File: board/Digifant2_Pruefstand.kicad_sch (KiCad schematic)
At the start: 71 parts, among them J0 VW ECU HARNESS, J1 12V BENCH IN, J2 IDLE VALVE N71, J3 OLED / UI I2C, Q1 2N7002, Q2 P-MOS -30V >=5A, Q3 2N7002, Q5 2N7002, SW1 PUSH, SW2 PUSH, SW3 PUSH, U1 INA226 (0x40), U2 MCP4728 (0x60), U3 INA226 (0x41), U4 AD9833, U5 Raspberry Pi Pico, U6 TS5A3159A, U7 TS5A3159A, U8 TS5A3159A, Y1 25MHz

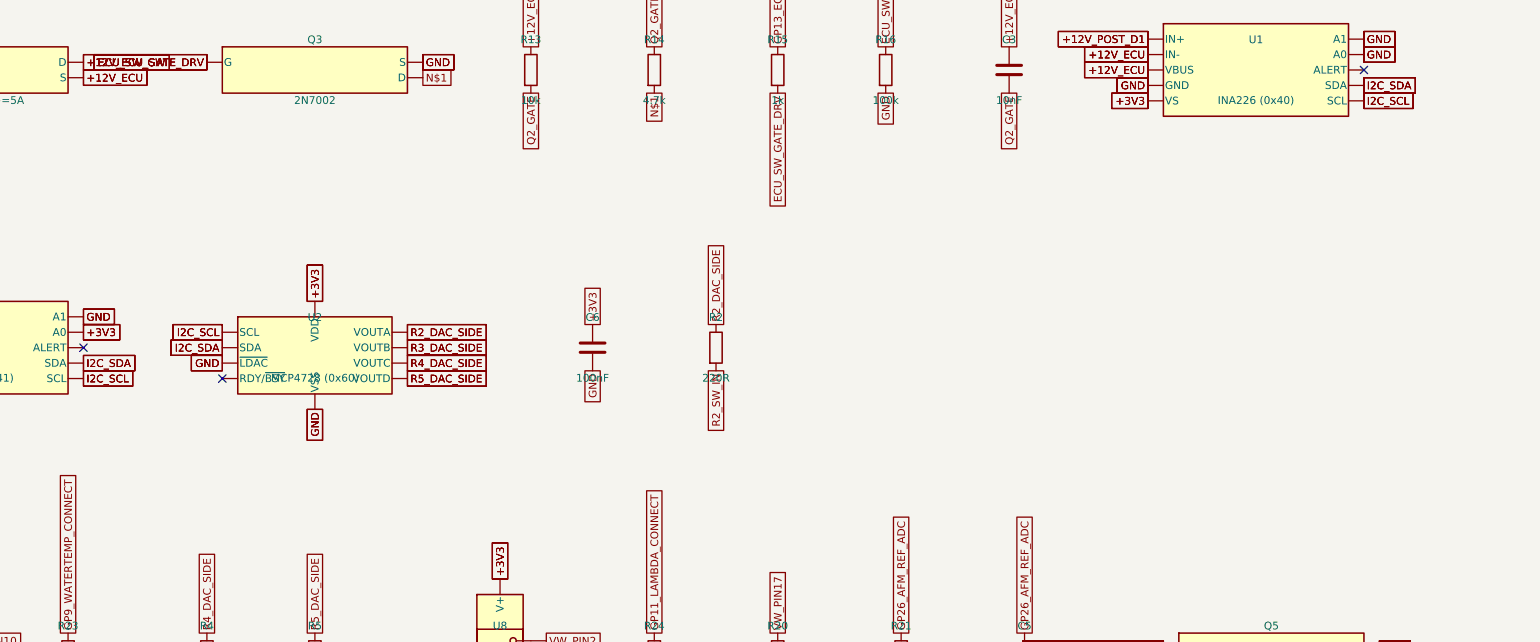
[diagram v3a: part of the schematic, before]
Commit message: Route remaining test points, add decoupling/thermal copper, trim board, label silkscreen
- Route TP7/TP8/TP9 (the three hardest, on U5's east side) with a purpose-built
  grid pathfinder after manual/Freerouting attempts kept snagging on the Pico's
  pin column, which has no usable gap anywhere along its length for a second
  trace; both had to detour around the south end of the module.
- Add C9/C10 (100nF) decoupling for U1/U3's VS pins per the INA226 datasheet,
  tapping the existing +3V3 trunk and GND pour near the packed U1/U3/RS1/RS2
  pocket.
- Add thermal copper pours for D1 (real risk: ~1.25W at sustained ~2.5A with
  no relief) and Q2, verified electrically connected via KiCad's connectivity
  API rather than just visually overlapping.
- Trim the board from 144x169mm to 144x150mm - the bottom 19mm was completely
  empty; move H3/H4 to keep the same edge margin as H1/H2.
- Add functional silkscreen labels next to J0 (real VW harness pin numbers)
  and every test point (moved from F.Fab, a documentation-only layer that
  never gets printed, to real F.SilkS; shortened long labels to fit the
  west-margin corridor without running off the board edge).
- Add fab-identification text (title/rev/date/company) to the previously
  empty back silkscreen, driven by the board's title block variables.
- Fix all 14 test points having "Exclude from BOM" set on the PCB side
  (schematic-parity check caught it) - they're real parts, not mechanical-only.
- Refill the GND zone after all of the above; confirmed the earlier
  "whole-board refill causes spurious violations" finding was a testing
  artifact (missing paired .kicad_pro), not a real issue.
- Regenerate the InteractiveHtmlBom output to include the newly-un-excluded
  test points.

Co-Authored-By: Claude Sonnet 5 <noreply@anthropic.com>
Claude-Session: https://claude.ai/code/session_01XcEuUwwCT37oProAm8HYeY
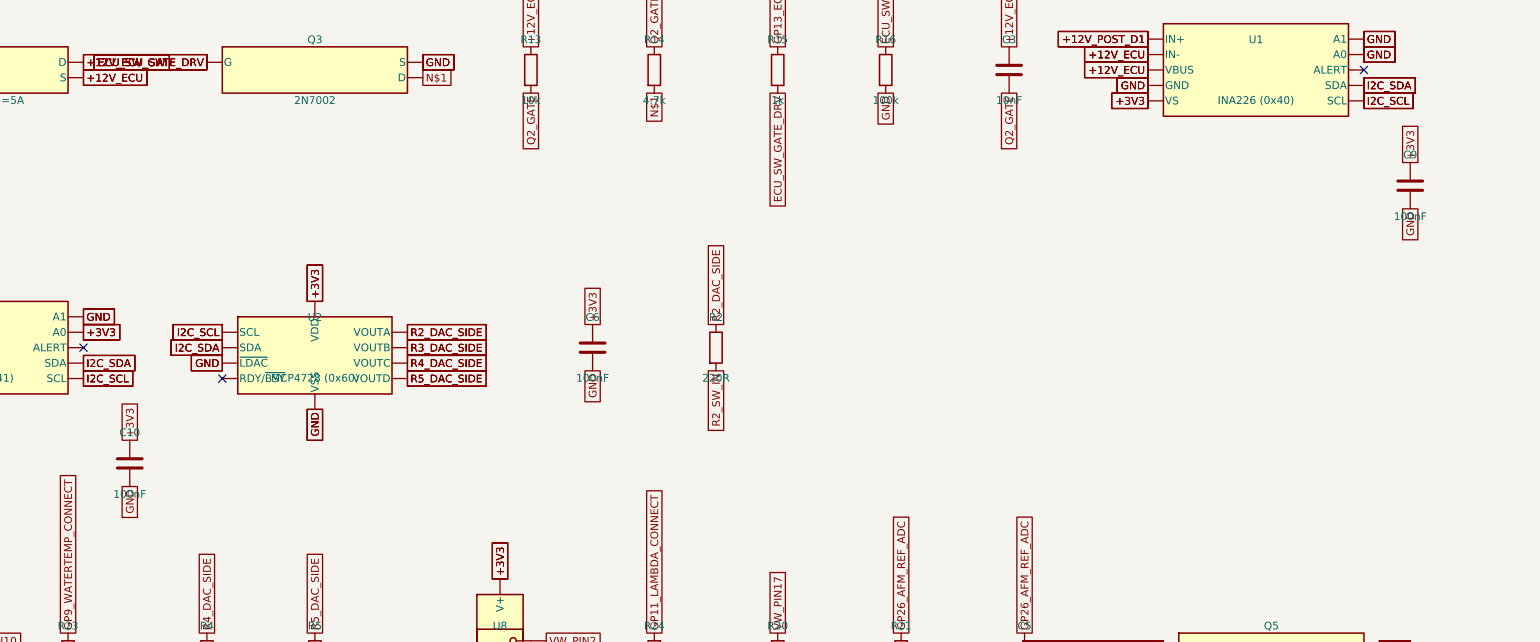
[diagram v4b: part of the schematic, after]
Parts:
- added C10, C9: 100nF, Capacitor_SMD:C_0805_2012Metric, symbol Device:C
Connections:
- net +3V3: now also C10.1, C9.1
- net GND: now also C10.2, C9.2
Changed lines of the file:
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@@
+		)
+	)
+	(symbol
+		(lib_id Device:C)
+		(at 368.3 120.65 0)
+		(in_bom yes)
+		(on_board yes)
+		(dnp no)
+		(property
+			"Reference"
+			"C9"
+			(at 368.3 115.57000000000001 0)
+			(effects
+				(font
+					(size 1.27 1.27)
+				)
+			)
+		)
+		(property
+			"Value"
+			"100nF"
+			(at 368.3 125.73 0)
+			(effects
+				(font
+					(size 1.27 1.27)
+				)
+			)
+		)
+		(property
+			"Footprint"
+			"Capacitor_SMD:C_0805_2012Metric"
+			(at 368.3 130.81 0)
+			(effects
+				(font
+					(size 1.27 1.27)
+				)
+				(hide yes)
+			)
+		)
+		(instances
+			(project
+				"circuit"
+				(path
+					"/"
+					(reference C9)
+					(unit 1)
+				)
+			)
+		)
+	)
+	(global_label
+		+3V3
+		(at 368.3 116.84 90)
+		(effects
+			(font
+				(size 1.27 1.27)
+			)
+			(justify left)
+		)
+	)
+	(global_label
+		GND
+		(at 368.3 124.46000000000001 270)
+		(effects
+			(font
+				(size 1.27 1.27)
+			)
+			(justify right)
+		)
+	)
+	(symbol
+		(lib_id Device:C)
+		(at 157.48 166.37 0)
+		(in_bom yes)
+		(on_board yes)
+		(dnp no)
+		(property
+			"Reference"
+			"C10"
+			(at 157.48 161.29 0)
+			(effects
+				(font
+					(size 1.27 1.27)
+				)
+			)
+		)
+		(property
+			"Value"
+			"100nF"
+			(at 157.48 171.45000000000002 0)
+			(effects
+				(font
+					(size 1.27 1.27)
+				)
+			)
+		)
+		(property
+			"Footprint"
+			"Capacitor_SMD:C_0805_2012Metric"
+			(at 157.48 176.53 0)
+			(effects
+				(font
+					(size 1.27 1.27)
+				)
+				(hide yes)
+			)
+		)
+		(instances
+			(project
+				"circuit"
+				(path
+					"/"
+					(reference C10)
+					(unit 1)
+				)
+			)
+		)
+	)
+	(global_label
+		+3V3
+		(at 157.48 162.56 90)
+		(effects
+			(font
+				(size 1.27 1.27)
+			)
+			(justify left)
+		)
+	)
+	(global_label
+		GND
+		(at 157.48 170.18 270)
+		(effects
+			(font
+				(size 1.27 1.27)
+			)
+			(justify right)
 		)
 	)

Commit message: Apply the two bring-up fixes to the live schematic/PCB; update docs
U6/U7/U8 COM-to-NC fix and R10 = 220R, hand-edited directly in
board/*.kicad_sch and board/*.kicad_pcb (not a circuit-synth
regeneration, which would discard the hand-routing/GND pour). Verified
both ways before committing:
- ERC unchanged: same 66 warnings, same categories, 0 errors
- DRC with schematic-parity unchanged: 112 violations in the same four
  pre-existing categories, 48 schematic-parity issues, 0 unconnected
  items -- an intermediate pass surfaced one new via_dangling at U8
  pad 4 (an incomplete layer-change via from the reroute), fixed and
  reverted to the clean baseline before this commit
- U6/U7/U8 pad 4 (COM) now carries the VW net, pad 3 (NC) is open;
  R10 is 220R, still wired straight between +3V3 and VW-12

DESIGN.md and BRINGUP.md updated to say so, while keeping the bodge
instructions for the board already fabricated and in bring-up -- the
live files fix the *design*, not the physical board already printed.
Revision intentionally left as-is: more bring-up findings are still
expected before the next fab run.

Co-Authored-By: Claude Sonnet 5 <noreply@anthropic.com>
Claude-Session: https://claude.ai/code/session_01XcEuUwwCT37oProAm8HYeY
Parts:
- R10: value 1k -> 220R
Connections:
- net VW_PIN10: now also U7.4; no longer U7.3
- net VW_PIN2: now also U8.4; no longer U8.3
- net VW_PIN9: now also U6.4; no longer U6.3
